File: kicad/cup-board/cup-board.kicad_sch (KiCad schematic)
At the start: 99 parts, among them J2 EARCUP_SPKR, J7 CUP_IN (A2B + panel audio, ma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, J8 CUP_OUT (A2B to next cup), Q1 AO3401A, Q2 MMBT3904, U1 ADAU1861, U2 LSM6DSV16BX, U3 MAXM86161, U4 AQW612S, U5 AQW612S, U6 AD2428WBCPZ (sub-node), U7 TPS62161DSG (1V8), U8 ADP7118AUJZ-3.3-R7 (3V3_MIC), U9 ADP7118AUJZ-3.3-R7 (VLED)

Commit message: [LIMA] cup board: MAXM86161 footprint from Maxim 90-100106 - all 99 parts done
U3 footprint drawn from Maxim land pattern 90-100106 rev A (pads 0.660x0.400,
pitch 0.600, columns 1.900) and outline 21-100309 rev B (pin order, body
2.9x4.3), both fetched from mds.analog.com. Pins 6/7/8 solder-only.

Checked: netlist == design_nets.py, ERC 0 errors, pin/pad parity 0
mismatches across all 99 parts.

Correction: d93b17f said "116 of 117 parts" - that was the audio board's
count. The cup board has 99 parts; 98 then, 99 now.

Co-Authored-By: Claude Opus 5.5 <noreply@anthropic.com>
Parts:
- U3: footprint (none) -> AnalogDevices:Maxim_OLGA-14_2.9x4.3mm_P0.6mm_F142A4_MAXM86161
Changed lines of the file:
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@@
 			)
 		)
-		(property "Footprint" ""
+		(property "Footprint" "AnalogDevices:Maxim_OLGA-14_2.9x4.3mm_P0.6mm_F142A4_MAXM86161"
 			(at 300.99 226.06 0)
 			(hide yes)

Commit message: [LIMA] cup PCB: M2 holes H1-H3 in schematic, In1 (power) / In2 (mixed) layers
Co-Authored-By: Claude Opus 5.5 <noreply@anthropic.com>
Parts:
- added H1, H2, H3: M2, MountingHole:MountingHole_2.2mm_M2, symbol Mechanical:MountingHole
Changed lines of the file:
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@@
 		)
 	)
-  (label "XF_SEC_A"
-    (at 490.22 226.06 180)
-    (fields_autoplaced yes)
-    (effects (font (size 1.27 1.27)) (justify right bottom))
-  )
-  (label "XF_SEC_B"
-    (at 490.22 228.60000000000002 180)
-    (fields_autoplaced yes)
-    (effects (font (size 1.27 1.27)) (justify right bottom))
-  )
-  (label "PPG_INT"
-    (at 431.8 111.76 0)
-    (fields_autoplaced yes)
-    (effects (font (size 1.27 1.27)) (justify left bottom))
-  )
+	(label "XF_SEC_A"
+		(at 490.22 226.06 180)
+		(effects
+			(font
+				(size 1.27 1.27)
+			)
+			(justify right bottom)
+		)
+	)
+	(label "XF_SEC_B"
+		(at 490.22 228.6 180)
+		(effects
+			(font
+				(size 1.27 1.27)
+			)
+			(justify right bottom)
+		)
+	)
+	(label "PPG_INT"
+		(at 431.8 111.76 0)
+		(effects
+			(font
+				(size 1.27 1.27)
+			)
+			(justify left bottom)
+		)
+	)
 	(symbol
 		(lib_id "AnalogDevices:ADAU1861")
@@
 					(unit 1)
 				)
+			)
+		)
+	)
+	(symbol
+		(lib_id "Mechanical:MountingHole")
+		(at 120.65 393.7 0)
+		(unit 1)
+		(in_bom yes)
+		(on_board yes)
+		(dnp no)
+		(property "Reference" "H1"
+			(at 120.65 388.62 0)
+			(effects
+				(font
+					(size 1.27 1.27)
+				)
+			)
+		)
+		(property "Value" "M2"
+			(at 120.65 390.525 0)
+			(effects
+				(font
+					(size 1.27 1.27)
+				)
+			)
+		)
+		(property "Footprint" "MountingHole:MountingHole_2.2mm_M2"
+			(at 120.65 393.7 0)
+			(hide yes)
+			(effects
+				(font
+					(size 1.27 1.27)
+				)
+			)
+		)
+		(property "Datasheet" ""
+			(at 120.65 393.7 0)
+			(hide yes)
+			(effects
+				(font
+					(size 1.27 1.27)
+				)
+			)
+		)
+		(instances
+			(project "cup-board"
+				(path "790ac8fa-b8c8-432b-bc66-3eedd04170ff"
+					(reference "H1")
+					(unit 1)
+				)
+			)
+		)
+	)
+	(symbol
+		(lib_id "Mechanical:MountingHole")
+		(at 135.89 393.7 0)
+		(unit 1)
+		(in_bom yes)
+		(on_board yes)
+		(dnp no)
+		(property "Reference" "H2"
+			(at 135.89 388.62 0)
+			(effects
+				(font
+					(size 1.27 1.27)
+				)
+			)
+		)
+		(property "Value" "M2"
+			(at 135.89 390.525 0)
+			(effects
+				(font
+					(size 1.27 1.27)
+				)
+			)
+		)
+		(property "Footprint" "MountingHole:MountingHole_2.2mm_M2"
+			(at 135.89 393.7 0)
+			(hide yes)
+			(effects
+				(font
+					(size 1.27 1.27)
+				)
+			)
+		)
+		(property "Datasheet" ""
+			(at 135.89 393.7 0)
+			(hide yes)
+			(effects
+				(font
+					(size 1.27 1.27)
+				)
+			)
+		)
+		(instances
+			(project "cup-board"
+				(path "790ac8fa-b8c8-432b-bc66-3eedd04170ff"
+					(reference "H2")
+					(unit 1)
+				)
+			)
+		)
+	)
+	(symbol
+		(lib_id "Mechanical:MountingHole")
+		(at 151.13 393.7 0)
+		(unit 1)
+		(in_bom yes)
+		(on_board yes)
+		(dnp no)
+		(property "Reference" "H3"
+			(at 151.13 388.62 0)
+			(effects
+				(font
+					(size 1.27 1.27)
+				)
+			)
+		)
+		(property "Value" "M2"
+			(at 151.13 390.525 0)
+			(effects
+				(font
+					(size 1.27 1.27)
+				)
+			)
+		)
+		(property "Footprint" "MountingHole:MountingHole_2.2mm_M2"
+			(at 151.13 393.7 0)
+			(hide yes)
+			(effects
+				(font
+					(size 1.27 1.27)
+				)
+			)
+		)
+		(property "Datasheet" ""
+			(at 151.13 393.7 0)
+			(hide yes)
+			(effects
+				(font
+					(size 1.27 1.27)
+				)
+			)
+		)
+		(instances
+			(project "cup-board"
+				(path "790ac8fa-b8c8-432b-bc66-3eedd04170ff"
+					(reference "H3")
+					(unit 1)
+				)

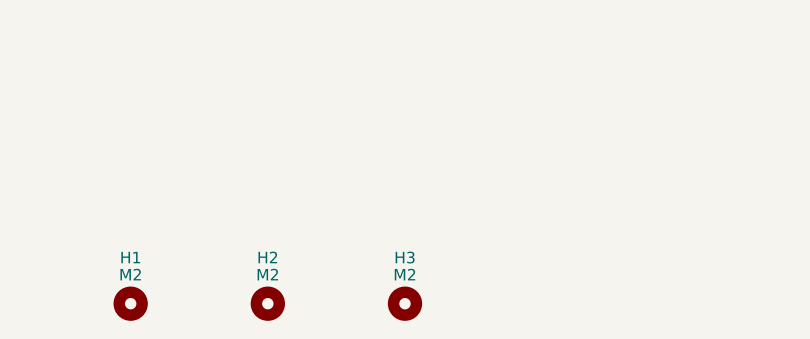
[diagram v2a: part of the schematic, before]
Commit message: [LIMA] cup board: H3 removed (Peter - two M2 holes is fine); it blocked the top routing corridor
Schematic via Konnect delete_schematic_component; footprint via pcbnew (KiCad closed). Parity 0.

Co-Authored-By: Claude Opus 5.5 <noreply@anthropic.com>
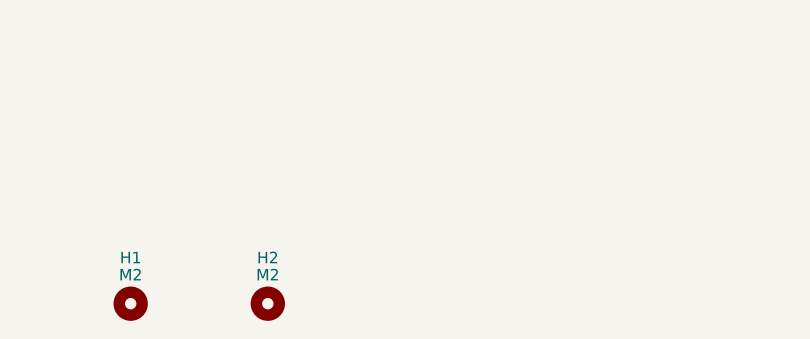
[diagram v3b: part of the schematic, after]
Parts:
- removed H3: M2, MountingHole:MountingHole_2.2mm_M2, symbol Mechanical:MountingHole
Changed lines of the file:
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@@
-		)
-	)
-	(symbol
-		(lib_id "Mechanical:MountingHole")
-		(at 151.13 393.7 0)
-		(unit 1)
-		(in_bom yes)
-		(on_board yes)
-		(dnp no)
-		(property "Reference" "H3"
-			(at 151.13 388.62 0)
-			(effects
-				(font
-					(size 1.27 1.27)
-				)
-			)
-		)
-		(property "Value" "M2"
-			(at 151.13 390.525 0)
-			(effects
-				(font
-					(size 1.27 1.27)
-				)
-			)
-		)
-		(property "Footprint" "MountingHole:MountingHole_2.2mm_M2"
-			(at 151.13 393.7 0)
-			(hide yes)
-			(effects
-				(font
-					(size 1.27 1.27)
-				)
-			)
-		)
-		(property "Datasheet" ""
-			(at 151.13 393.7 0)
-			(hide yes)
-			(effects
-				(font
-					(size 1.27 1.27)
-				)
-			)
-		)
-		(instances
-			(project "cup-board"
-				(path "790ac8fa-b8c8-432b-bc66-3eedd04170ff"
-					(reference "H3")
-					(unit 1)
-				)
-			)
 		)
 	)

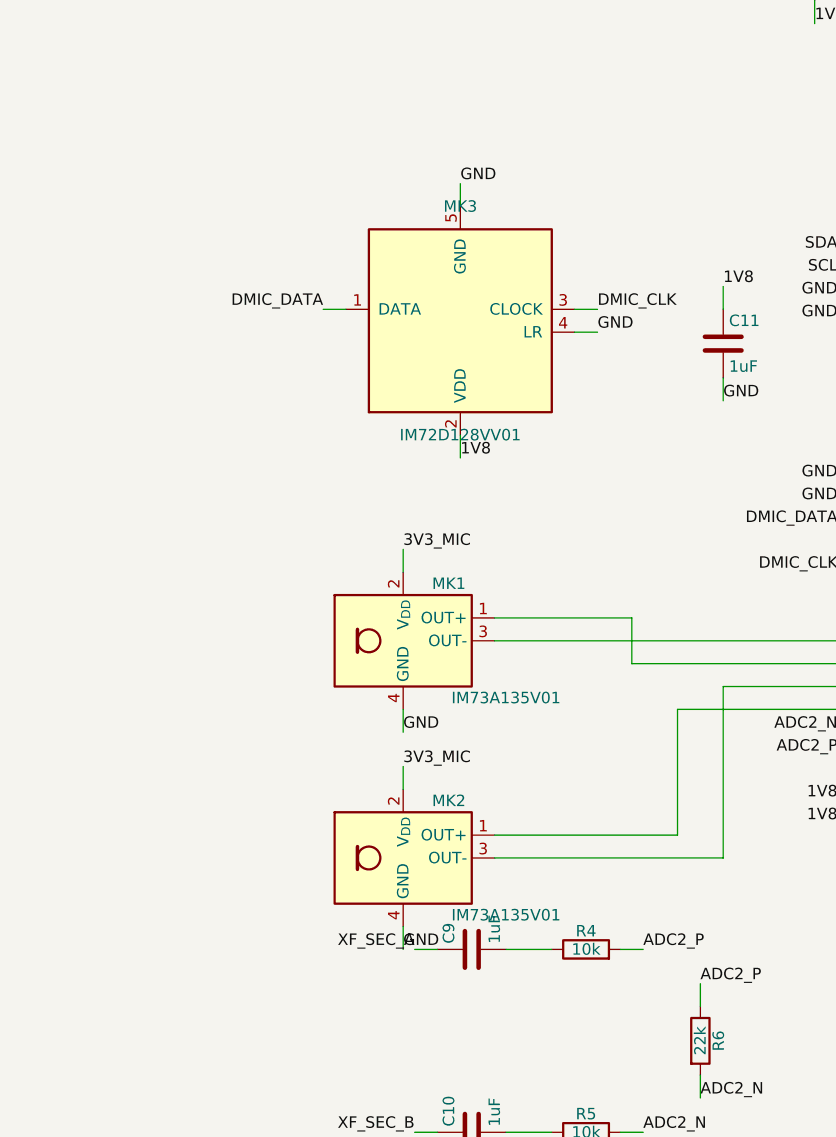
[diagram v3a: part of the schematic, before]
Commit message: [LIMA] cup schematic: mics moved to Infineon flex eval boards (Peter) - MK1/MK2/MK3 -> J9/J10/J11 6-pin 0.5 mm ZIF
Hirose FH12-6S-0.5SH (stock KiCad footprint + 3D). Nets renamed MK1_OUTP/N, MK2_OUTP/N; DMIC_DATA/CLK kept;
J11.4 (PDM SELECT) tied low as MK3 LR was. Contact order is a PLACEHOLDER from Infineon's 2020 flex-adapter
table (1 VDD, 2 DATA/OUT+, 3 CLK/OUT-, 4 SEL/nc, 5-6 GND) - the flex tail order isn't public; verify on the kit
before fab (Note field on each connector). ERC 0 errors; netlist == design_nets.py.

Co-Authored-By: Claude Opus 5.5 <noreply@anthropic.com>
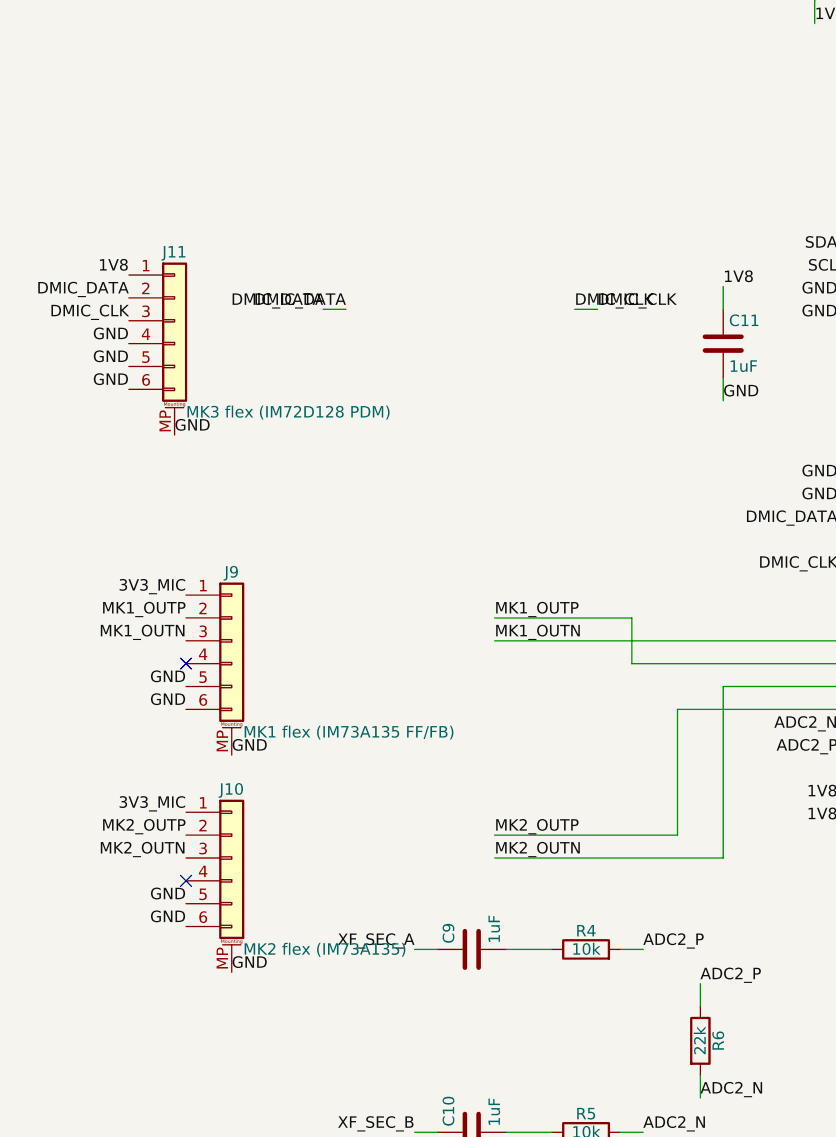
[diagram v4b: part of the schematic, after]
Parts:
- removed MK1, MK2: IM73A135V01, Infineon:Infineon_PG-LLGA-5_4x3mm_IM73A135_IM72D128, symbol Sensor_Audio:IM73A135V01
- removed MK3: IM72D128VV01, Infineon:Infineon_PG-LLGA-5_4x3mm_IM73A135_IM72D128, symbol Infineon:IM72D128V
- added J10: MK2 flex (IM73A135), Connector_FFC-FPC:Hirose_FH12-6S-0.5SH_1x06-1MP_P0.50mm_Horizontal, symbol Connector_Generic_MountingPin:Conn_01x06_MountingPin
- added J11: MK3 flex (IM72D128 PDM), Connector_FFC-FPC:Hirose_FH12-6S-0.5SH_1x06-1MP_P0.50mm_Horizontal, symbol Connector_Generic_MountingPin:Conn_01x06_MountingPin
- added J9: MK1 flex (IM73A135 FF/FB), Connector_FFC-FPC:Hirose_FH12-6S-0.5SH_1x06-1MP_P0.50mm_Horizontal, symbol Connector_Generic_MountingPin:Conn_01x06_MountingPin
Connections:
- net 1V8: now also J11.1 (Pin_1)
- net 3V3_MIC: now also J10.1 (Pin_1), J9.1 (Pin_1)
- net DMIC_CLK: now also J11.3 (Pin_3)
- net DMIC_DATA: now also J11.2 (Pin_2)
- net GND: now also J10.5 (Pin_5), J10.6 (Pin_6), J10.MP (MountPin), J11.4 (Pin_4), J11.5 (Pin_5), J11.6 (Pin_6), J11.MP (MountPin), J9.5 (Pin_5), J9.6 (Pin_6), J9.MP (MountPin)
- net MK1_OUTP: now reaches U1.20 (AINP0)
- net MK1_OUTP: now also J9.2 (Pin_2)
- net MK1_OUTN: now reaches U1.19 (AINN0)
- net MK1_OUTN: now also J9.3 (Pin_3)
- net MK2_OUTP: now reaches U1.22 (AINP1)
- net MK2_OUTP: now also J10.2 (Pin_2)
- net MK2_OUTN: now reaches U1.21 (AINN1)
- net MK2_OUTN: now also J10.3 (Pin_3)
- no-connect marks 37 -> 39

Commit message: [LIMA] schematics: boom electret pass-through via the cups (Peter)
Cup: J12 2-pin boom electret in -> J7.5/J7.6 (J7 now 6-pin SM06B). ELEC_HI/ELEC_LO touch nothing else on the cup.
Audio: J3 6-pin (5/6 = ELEC_HI/LO from cup L), J4 4-pin (3/4 = ELEC_HI/LO from cup R), joined to the existing J6/K1 nets.
Netlist == design files on both; ERC warnings unchanged (pin-type only).

Co-Authored-By: Claude Opus 5.5 <noreply@anthropic.com>
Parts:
- added J12: BOOM_ELECTRET (pass-through to audio K1), Connector_JST:JST_GH_SM02B-GHS-TB_1x02-1MP_P1.25mm_Horizontal, symbol Connector_Generic:Conn_01x02
- J7: value CUP_IN (A2B + panel audio, mates audio J3) -> CUP_IN (A2B + panel audio + boom electret, mates audio J3 / J4); footprint Connector_JST:JST_GH_SM04B-GHS-TB_1x04-1MP_P1.25mm_Horizontal -> Connector_JST:JST_GH_SM06B-GHS-TB_1x06-1MP_P1.25mm_Horizontal; symbol Connector_Generic:Conn_01x04 -> Connector_Generic:Conn_01x06
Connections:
- new net ELEC_HI: J12.1 (Pin_1), J7.5 (Pin_5)
- new net ELEC_LO: J12.2 (Pin_2), J7.6 (Pin_6)
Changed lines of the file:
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@@
 		)
 	)
+	(wire
+		(pts
+			(xy 490.22 231.14)
+			(xy 487.68 231.14)
+		)
+	)
+	(wire
+		(pts
+			(xy 490.22 233.68)
+			(xy 487.68 233.68)
+		)
+	)
+	(wire
+		(pts
+			(xy 490.22 246.38)
+			(xy 487.68 246.38)
+		)
+	)
+	(wire
+		(pts
+			(xy 490.22 248.92)
+			(xy 487.68 248.92)
+		)
+	)
 	(text "A2B SUB-NODE (2026-10-23, per Peter): U6 AD2428, bus-powered (AD242x DS Fig. 36; coupling per EVAL-AD2428WD1BZ sheet 2)\nA side J7 (from AeroNode or previous cup): line+ -> L3 -> V_NODE -> D1 -> VIN_CUP; line- -> L4 -> GND (this cup's ground is the recovered bus bias).\nB side J8 (to next cup, unused on the last cup): V_NODE -> R12 -> Q1 (gate: SWP via R13) -> L5 -> line+; line- -> L6 -> VSSN. SENSE via R14.\nI2S: U6 is master. DTX0 -> I2S0_SDATAI (ADAU1861 in), DRX0 <- I2S0_SDATAO. I2C: U6 masters SDA/SCL at 1V8 (IOVDD = 1V8).\nK2: AudioBoard CTL_SPKR -> main IO7 -> GPIO-over-distance -> U6 IO7 -> K2_CTL -> Q2 -> U4/U5 LEDs (R7/R8 680R from VIN_CUP). Default off.\nPower from VIN_CUP (6.4-7.2 V with the AeroNode's 8 V bus): U7 TPS62161 -> 1V8; U8 ADP7118 -> 3V3_MIC; U9 ADP7118 -> VLED.\nEE-419: a bus-powered node's ground is offset from the AeroNode's - connect only floating signals (J5 is transformer-isolated, AC-coupled).\nBudget: docs/a2b-bus-power-budget.md - cup R VIN 6.44 V worst case on the 8 V bus (3.7 V min)."
 		(at 475 285 0)
@@
 		)
 	)
+	(label "ELEC_HI"
+		(at 487.68 231.14 180)
+		(effects
+			(font
+				(size 1.27 1.27)
+			)
+			(justify right bottom)
+		)
+	)
+	(label "ELEC_LO"
+		(at 487.68 233.68 180)
+		(effects
+			(font
+				(size 1.27 1.27)
+			)
+			(justify right bottom)
+		)
+	)
+	(label "ELEC_HI"
+		(at 487.68 246.38 180)
+		(effects
+			(font
+				(size 1.27 1.27)
+			)
+			(justify right bottom)
+		)
+	)
+	(label "ELEC_LO"
+		(at 487.68 248.92 180)
+		(effects
+			(font
+				(size 1.27 1.27)
+			)
+			(justify right bottom)
+		)
+	)
 	(symbol
 		(lib_id "AnalogDevices:ADAU1861")
@@
 	)
 	(symbol
-		(lib_id "Connector_Generic:Conn_01x04")
-		(at 495.3 223.52 0)
+		(lib_id "Connector_Generic:Conn_01x06")
+		(at 495.3 226.06 0)
 		(unit 1)
 		(in_bom yes)
@@
 		(dnp no)
 		(property "Reference" "J7"
-			(at 495.3 218.44 0)
+			(at 495.3 220.98 0)
 			(effects
 				(font
@@
 			)
 		)
-		(property "Value" "CUP_IN (A2B + panel audio, mates audio J3)"
-			(at 495.3 231.14 0)
+		(property "Value" "CUP_IN (A2B + panel audio + boom electret, mates audio J3 / J4)"
+			(at 495.3 233.68 0)
 			(effects
 				(font
@@
 			)
 		)
-		(property "Footprint" "Connector_JST:JST_GH_SM04B-GHS-TB_1x04-1MP_P1.25mm_Horizontal"
-			(at 495.3 223.52 0)
+		(property "Footprint" "Connector_JST:JST_GH_SM06B-GHS-TB_1x06-1MP_P1.25mm_Horizontal"
+			(at 495.3 226.06 0)
 			(hide yes)
 			(effects
@@
 		)
 		(property "Datasheet" ""
-			(at 495.3 223.52 0)
+			(at 495.3 226.06 0)
 			(hide yes)
 			(effects
@@
 			)
 		)
-		(instances
-			(project "cup-board"
-				(path "/790ac8fa-b8c8-432b-bc66-3eedd04170ff"
-					(reference "J9")
-					(unit 1)
-				)
-			)
-		)
 		(property "MPN" "Hirose FH12-6S-0.5SH(55)"
 			(at 95.25 151.13 0)
@@
 				)
 			)
-		))
+		)
+		(instances
+			(project "cup-board"
+				(path "/790ac8fa-b8c8-432b-bc66-3eedd04170ff"
+					(reference "J9")
+					(unit 1)
+				)
+			)
+		)
+	)
 	(symbol
 		(lib_id "Connector_Generic_MountingPin:Conn_01x06_MountingPin")
@@
 			)
 		)
-		(instances
-			(project "cup-board"
-				(path "/790ac8fa-b8c8-432b-bc66-3eedd04170ff"
-					(reference "J10")
-					(unit 1)
-				)
-			)
-		)
 		(property "MPN" "Hirose FH12-6S-0.5SH(55)"
 			(at 95.25 175.26 0)
@@
 				)
 			)
-		))
+		)
+		(instances
+			(project "cup-board"
+				(path "/790ac8fa-b8c8-432b-bc66-3eedd04170ff"
+					(reference "J10")
+					(unit 1)
+				)
+			)
+		)
+	)
 	(symbol
 		(lib_id "Connector_Generic_MountingPin:Conn_01x06_MountingPin")
@@
 			)
 		)
+		(property "MPN" "Hirose FH12-6S-0.5SH(55)"
+			(at 88.9 115.57 0)
+			(hide yes)
+			(effects
+				(font
+					(size 1.27 1.27)
+				)
+			)
+		)
+		(property "Note" "PINOUT PLACEHOLDER (Infineon 2020 adapter order 1 VDD, 2 DATA, 3 CLK, 4 SELECT=GND, 5-6 GND) - verify against KIT_IM72D128V01_FLEX flex tail before fab"
+			(at 88.9 115.57 0)
+			(hide yes)
+			(effects
+				(font
+					(size 1.27 1.27)
+				)
+			)
+		)
 		(instances
 			(project "cup-board"
@@
 			)
 		)
-		(property "MPN" "Hirose FH12-6S-0.5SH(55)"
-			(at 88.9 115.57 0)
+	)
+	(symbol
+		(lib_id "Connector_Generic:Conn_01x02")
+		(at 495.3 246.38 0)
+		(unit 1)
+		(in_bom yes)
+		(on_board yes)
+		(dnp no)
+		(property "Reference" "J12"
+			(at 495.3 243.84 0)
+			(effects
+				(font
+					(size 1.27 1.27)
+				)
+			)
+		)
+		(property "Value" "BOOM_ELECTRET (pass-through to audio K1)"
+			(at 495.3 251.46 0)
+			(effects
+				(font
+					(size 1.27 1.27)
+				)
+			)
+		)
+		(property "Footprint" "Connector_JST:JST_GH_SM02B-GHS-TB_1x02-1MP_P1.25mm_Horizontal"
+			(at 495.3 246.38 0)
 			(hide yes)
 			(effects
@@
 			)
 		)
-		(property "Note" "PINOUT PLACEHOLDER (Infineon 2020 adapter order 1 VDD, 2 DATA, 3 CLK, 4 SELECT=GND, 5-6 GND) - verify against KIT_IM72D128V01_FLEX flex tail before fab"
-			(at 88.9 115.57 0)
+		(property "Datasheet" ""
+			(at 495.3 246.38 0)
+			(hide yes)
+			(effects
+				(font
+					(size 1.27 1.27)
+				)
+			)
+		)
+		(instances
+			(project "cup-board"
+				(path "/790ac8fa-b8c8-432b-bc66-3eedd04170ff"
+					(reference "J12")
+					(unit 1)
+				)
+			)
+		)
+		(property "Note" "Boom electret in. Aircraft-side circuit: console-biased, isolated from GND - no connection to anything on this board except J7.5/J7.6. Aircraft clearance class."
+			(at 495.3 246.38 0)
 			(hide yes)
 			(effects

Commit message: [LIMA] cup PCB: J7 -> 6-pin GH, J12 boom-electret solder pads (Peter), re-routed - 0 unconnected, 0 errors
J12 = two 0.15 mm2 wire pads at 311 deg (no room on the outer band for a GH; Peter chose pads). ELEC_HI/LO in a new
Aircraft netclass (0.5 mm), J12 -> J7.5/6 only. J7 nets re-routed by maze. One parity warning: J12 footprint is
exclude-from-BOM, the symbol is not (Konnect cannot set the symbol flag).

Co-Authored-By: Claude Opus 5.5 <noreply@anthropic.com>
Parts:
- J12: value BOOM_ELECTRET (pass-through to audio K1) -> BOOM_ELECTRET (solder pads, pass-through to audio K1); footprint Connector_JST:JST_GH_SM02B-GHS-TB_1x02-1MP_P1.25mm_Horizontal -> Connector_Wire:SolderWire-0.15sqmm_1x02_P4mm_D0.5mm_OD1.5mm
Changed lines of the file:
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@@
 			)
 		)
-		(property "Value" "BOOM_ELECTRET (pass-through to audio K1)"
+		(property "Value" "BOOM_ELECTRET (solder pads, pass-through to audio K1)"
 			(at 495.3 251.46 0)
 			(effects
@@
 			)
 		)
-		(property "Footprint" "Connector_JST:JST_GH_SM02B-GHS-TB_1x02-1MP_P1.25mm_Horizontal"
+		(property "Footprint" "Connector_Wire:SolderWire-0.15sqmm_1x02_P4mm_D0.5mm_OD1.5mm"
 			(at 495.3 246.38 0)
 			(hide yes)
